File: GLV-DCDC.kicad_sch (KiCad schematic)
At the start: 38 parts, among them IC1 LM34936QPWPTQ1, M1 NMOS_BTS141BKSA1, M2 NMOS_BTS141BKSA1, M3 NMOS_BTS141BKSA1, M4 NMOS_BTS141BKSA1

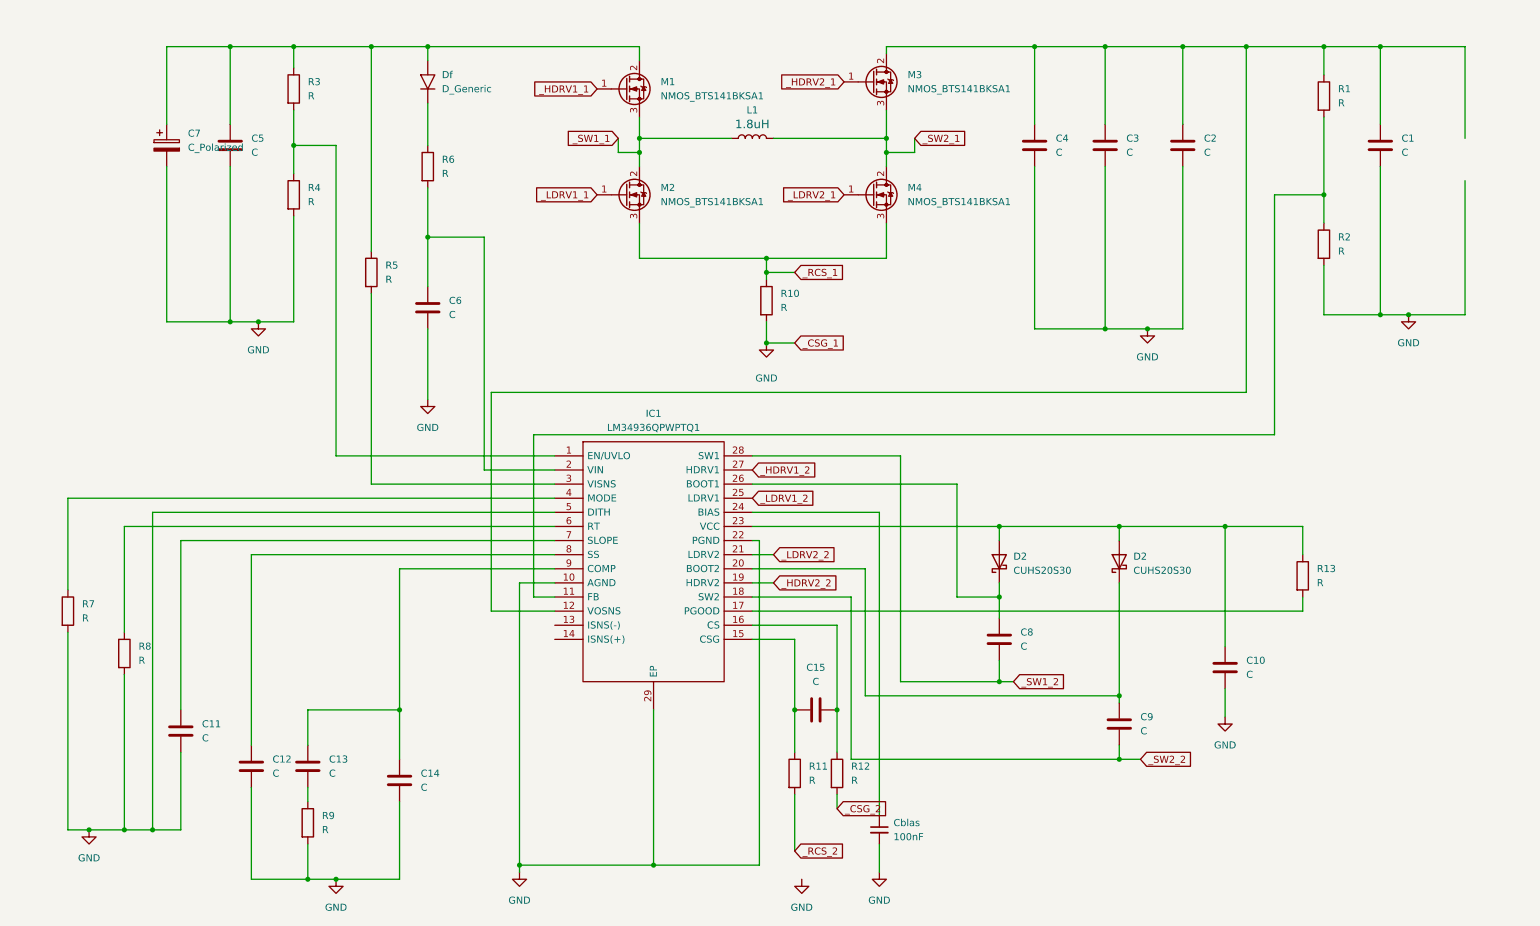
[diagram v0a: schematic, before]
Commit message: 回路作成
シンボルの修正と値を書き込みました
確認お願いします
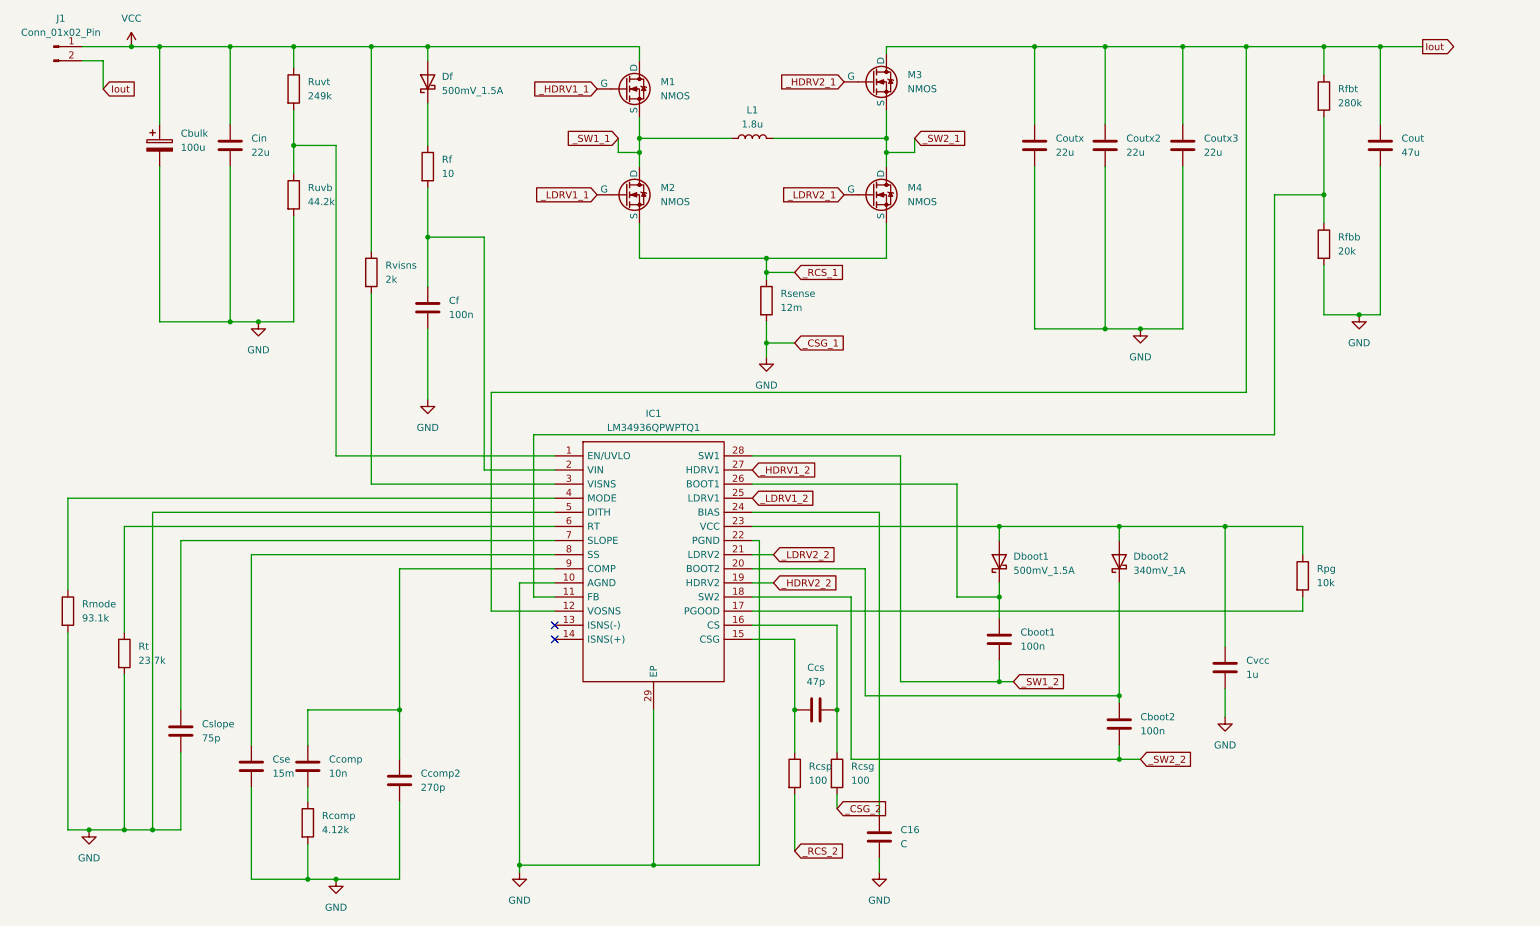
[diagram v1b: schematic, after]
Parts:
- removed Cblas: 100n, 4ms_Capacitor:C_0603, symbol PCM_4ms_Capacitor:C_Generic
- removed D2 (x2): CUHS20S30, SamacSys_Parts:CUHS20S40H3F, symbol Device:D_Schottky
- removed Df: D_Generic, symbol PCM_4ms_Diode:D_Generic
- removed L1: FerriteBead_0603_1.5A, 4ms_Resistor:R_0603, symbol PCM_4ms_Inductor:FerriteBead_0603_1.5A
- removed M1, M2, M3, M4: NMOS_BTS141BKSA1, 4ms_Package_TO:TO-220-3_Vertical, symbol PCM_4ms_Transistor:NMOS_BTS141BKSA1
- added C16: C, symbol Device:C
- added Dboot1, Df: 500mV_1.5A, symbol Device:D_Schottky
- added Dboot2: 340mV_1A, symbol Device:D_Schottky
- added J1: Conn_01x02_Pin, symbol Connector:Conn_01x02_Pin
- added L1: 1.8u, symbol Device:L
- added M1, M2, M3, M4: NMOS, symbol Simulation_SPICE:NMOS
- Cboot1: renamed from C8; value C -> 100n
- Cboot2: renamed from C9; value C -> 100n
- Cbulk: renamed from C7; value C_Polarized -> 100u
- Ccomp: renamed from C13; value C -> 10n
- Ccomp2: renamed from C14; value C -> 270p
- Ccs: renamed from C15; value C -> 47p
- Cf: renamed from C6; value C -> 100n
- Cin: renamed from C5; value C -> 22u
- Cout: renamed from C1; value C -> 47u
- Coutx: renamed from C4; value C -> 22u
- Coutx2: renamed from C3; value C -> 22u
- Coutx3: renamed from C2; value C -> 22u
- Cse: renamed from C12; value C -> 15m
- Cslope: renamed from C11; value C -> 75p
- Cvcc: renamed from C10; value C -> 1u
- Rcomp: renamed from R9; value R -> 4.12k
- Rcsg: renamed from R12; value R -> 100
- Rcsp: renamed from R11; value R -> 100
- Rf: renamed from R6; value R -> 10
- Rfbb: renamed from R2; value R -> 20k
- Rfbt: renamed from R1; value R -> 280k
- Rmode: renamed from R7; value R -> 93.1k
- Rpg: renamed from R13; value R -> 10k
- Rsense: renamed from R10; value R -> 12m
- Rt: renamed from R8; value R -> 23.7k
- Ruvb: renamed from R4; value R -> 44.2k
- Ruvt: renamed from R3; value R -> 249k
- Rvisns: renamed from R5; value R -> 2k
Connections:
- net GND: now also C16.2
- net _HDRV1_1: now also M1.2 (G)
- net _HDRV2_1: now also M3.2 (G)
- net _LDRV1_1: now also M2.2 (G)
- net _LDRV2_1: now also M4.2 (G)
- net _RCS_1: now also M2.3 (S), M4.3 (S)
- net _SW1_1: now also L1.1, M1.3 (S), M2.1 (D)
- net _SW2_1: now also L1.2, M3.3 (S), M4.1 (D)
- net Iout: now reaches Cout.1, Coutx.1, Coutx2.1, Coutx3.1, IC1.12 (VOSNS), Rfbt.1
- net Iout: now also J1.2 (Pin_2), M3.1 (D)
- net at Cboot2.1, IC1.20 (BOOT2): now also Dboot2.1 (K)
- net at Cvcc.1, IC1.23 (VCC), Rpg.1: now also Dboot1.2 (A), Dboot2.2 (A)
- net at IC1.24 (BIAS): now also C16.1
- net at Cboot1.1, IC1.26 (BOOT1): now also Dboot1.1 (K)
- net VCC: now reaches Cbulk.1, Cin.1, Ruvt.1, Rvisns.1
- net VCC: now also Df.2 (A), J1.1 (Pin_1), M1.1 (D)
- net at Rf.1: now also Df.1 (K)
- no-connect marks 0 -> 2
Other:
- moved on the sheet: Cbulk

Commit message: 回路図作成
訂正版です
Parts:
- removed Ccomp2: 270p, symbol Device:C
- removed Cf: 100n, symbol Device:C
- removed Cin, Coutx, Coutx2: 22u, symbol Device:C
- removed Cout: 47u, symbol Device:C
- added C1, C3, C4: 22u, symbol Device:C
- added C10: 270p, symbol Device:C
- added C2: 0.1u, symbol Device:C
- added C6: 47u, symbol Device:C_Polarized
- added J2: Conn_01x02_Pin, symbol Connector:Conn_01x02_Pin
- C12: renamed from Cboot1; value 100n -> 0.1u
- C13: renamed from Cboot2; value 100n -> 0.1u
- C15: renamed from C16; value C -> 0.1u
- renumbered Ccs to C11, Cvcc to C14, Cbulk to C16, Coutx3 to C5, Cslope to C7, Cse to C8, Ccomp to C9, Df to D1, Dboot1 to D2, Dboot2 to D3, Ruvt to R1, Rcomp to R10, Rcsp to R11, Rcsg to R12, Rpg to R13, Ruvb to R2, Rvisns to R3, Rf to R4, Rsense to R5, Rfbt to R6, Rfbb to R7, Rmode to R8, Rt to R9
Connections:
- net GND: now also J1.2 (Pin_2), C1.2, C10.2, C2.2, C3.2, C4.2, C6.2, J2.2 (Pin_2)
- net at IC1.2 (VIN), R4.2: now also C2.1
- net at C9.1, IC1.9 (COMP): now also C10.1
- net Iout renamed +12V
- net +12V: now also C3.1, C4.1, C6.1, J2.1 (Pin_1); no longer J1.2 (Pin_2)
- net VCC renamed VS
- net VS: now also C1.1
